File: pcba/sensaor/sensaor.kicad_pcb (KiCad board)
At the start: 2 copper layers, 55 x 29.5 mm, 16 parts, among them J1 SAO, J2 WS2812, J3 Conn_01x10_Pin, J4 Conn_01x10_Pin, J5 Conn_01x10_Pin, J6 Programming, J7 Conn_01x10_Pin, J8 Conn_01x10_Pin, J9 Conn_01x10_Pin, U1 CH32V003AxMx

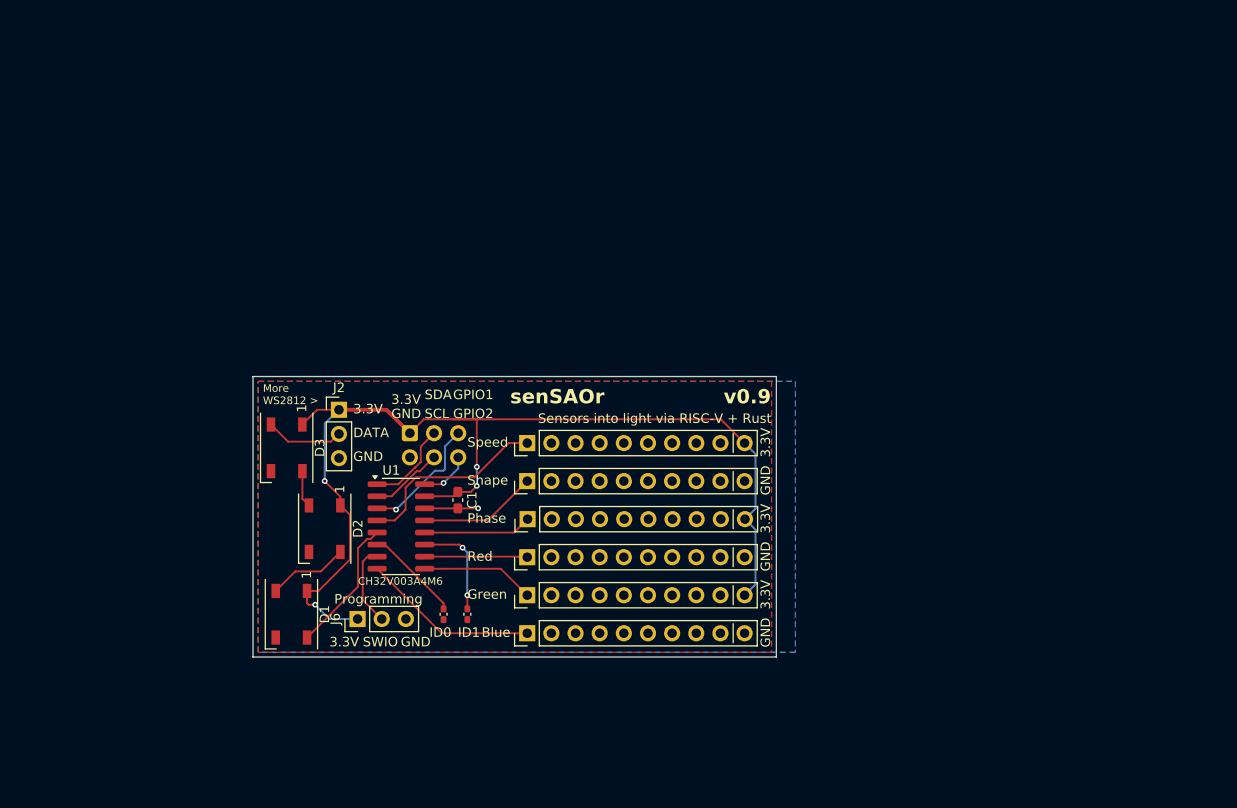
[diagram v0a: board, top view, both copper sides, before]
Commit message: Redesign board into more of a carrier shape
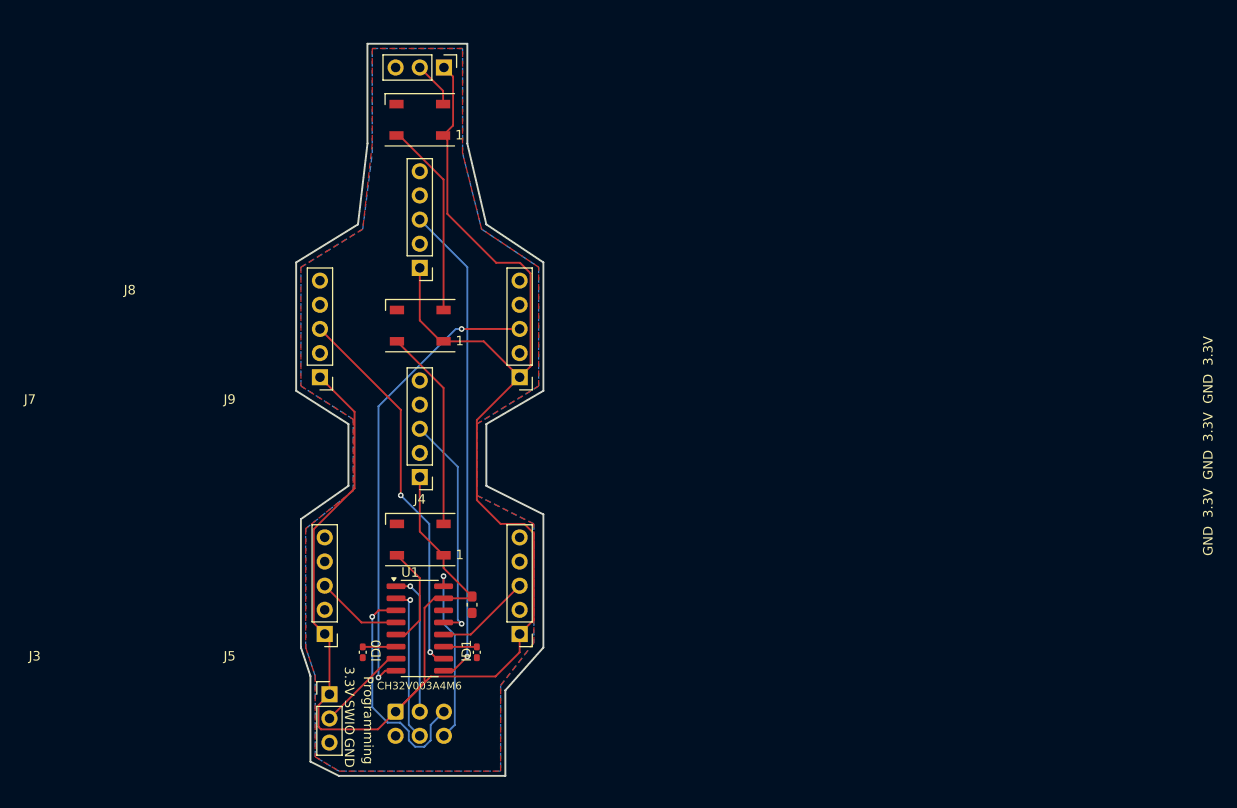
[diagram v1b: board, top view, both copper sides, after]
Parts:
- J3, J4, J5, J7, J8, J9: value Conn_01x10_Pin -> Conn_01x05_Pin; footprint Connector_PinHeader_2.54mm:PinHeader_1x10_P2.54mm_Vertical -> Connector_PinHeader_2.54mm:PinHeader_1x05_P2.54mm_Vertical
- moved J2 37.7 mm to (96.0, 20.5), turned to -90 degrees
- moved D3 37.2 mm to (93.5, 26.0), turned to 180 degrees
- moved J8 36.2 mm to (93.5, 41.6), turned to 180 degrees
- moved J1 29.3 mm to (91.0, 88.2)
- moved J3 29.3 mm to (83.5, 80.1), turned to 180 degrees
- moved J7 28.9 mm to (83.0, 53.1), turned to 180 degrees
- moved J9 26.9 mm to (104.0, 53.1), turned to 180 degrees
- moved D2 23.6 mm to (93.5, 47.6), turned to 180 degrees
- moved D1 15.7 mm to (93.5, 70.2), turned to 180 degrees
- moved J5 12.1 mm to (104.0, 80.1), turned to 180 degrees
- moved J4 11.3 mm to (93.5, 63.6), turned to 180 degrees
- moved C1 11.1 mm to (99.0, 77.0)
- moved U1 10.9 mm to (93.5, 79.5)
- moved R1 9.39 mm to (87.5, 82.0)
- moved J6 8.46 mm to (84.0, 86.4), turned to 0 degrees
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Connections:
- J3 pad 1: /SPEED -> VCC
- J3 pad 3: unconnected-(J3-Pin_3-Pad3) -> /SPEED
- J3 pad 5: unconnected-(J3-Pin_5-Pad5) -> GND
- J4 pad 1: /SHAPE -> VCC
- J4 pad 3: unconnected-(J4-Pin_3-Pad3) -> /SHAPE
- J4 pad 5: unconnected-(J4-Pin_5-Pad5) -> GND
- J5 pad 1: /PHASE -> VCC
- J5 pad 3: unconnected-(J5-Pin_3-Pad3) -> /PHASE
- J5 pad 5: unconnected-(J5-Pin_5-Pad5) -> GND
- J7 pad 1: /AR -> VCC
- J7 pad 3: unconnected-(J7-Pin_3-Pad3) -> /AR
- J7 pad 5: unconnected-(J7-Pin_5-Pad5) -> GND
- J8 pad 1: /AG -> VCC
- J8 pad 3: unconnected-(J8-Pin_3-Pad3) -> /AG
- J8 pad 5: unconnected-(J8-Pin_5-Pad5) -> GND
- J9 pad 1: /AB -> VCC
- J9 pad 3: unconnected-(J9-Pin_3-Pad3) -> /AB
- J9 pad 5: unconnected-(J9-Pin_5-Pad5) -> GND
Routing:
- net VCC: track 113.9 -> 192.3 mm, vias 4 -> 0
- net /AG: track 11.9 -> 51.1 mm, vias 0 -> 1
- net /AB: track 18.6 -> 48.9 mm, vias 0 -> 2
- net /AR: track 10.9 -> 40.5 mm, vias 0 -> 2
- net Net-(D2-DOUT): track 3.89 -> 20.6 mm
- net /GPIO2: track 5.37 -> 18.8 mm
- net Net-(D1-DOUT): track 8.50 -> 21.2 mm
- net /SHAPE: track 12.5 -> 24.3 mm, vias 0 -> 1
- net /SPEED: track 20.5 -> 9.10 mm
- net /GPIO1: track 13.3 -> 24.6 mm
- net /SCL: track 7.64 -> 16.4 mm, vias 0 -> 1
- net /ID1: track 10.9 -> 3.51 mm, vias 2 -> 0
- net GND: track 6.67 -> 0.00 mm, vias 1 -> 0
- net /ID0: track 10.1 -> 3.51 mm
- net /SDA: track 9.16 -> 15.1 mm, vias 0 -> 1
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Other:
- board size 55 x 29.5 mm -> 26 x 77 mm
- board text added: "v1.0"
- board text removed: "GPIO1"
- board text removed: "GPIO2"
- board text removed: "SCL"
- board text removed: "SDA"
- board text removed: "v0.9"

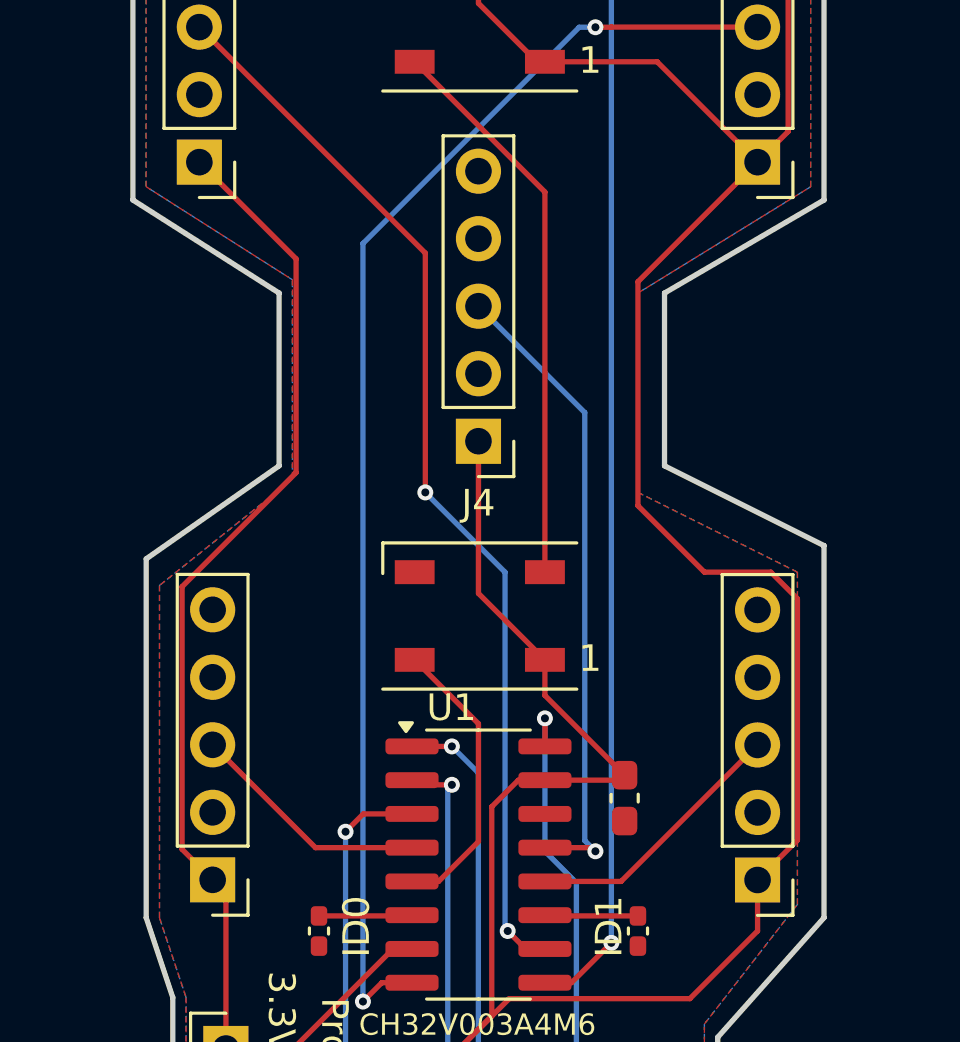
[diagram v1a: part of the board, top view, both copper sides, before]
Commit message: Fix ground plane connections
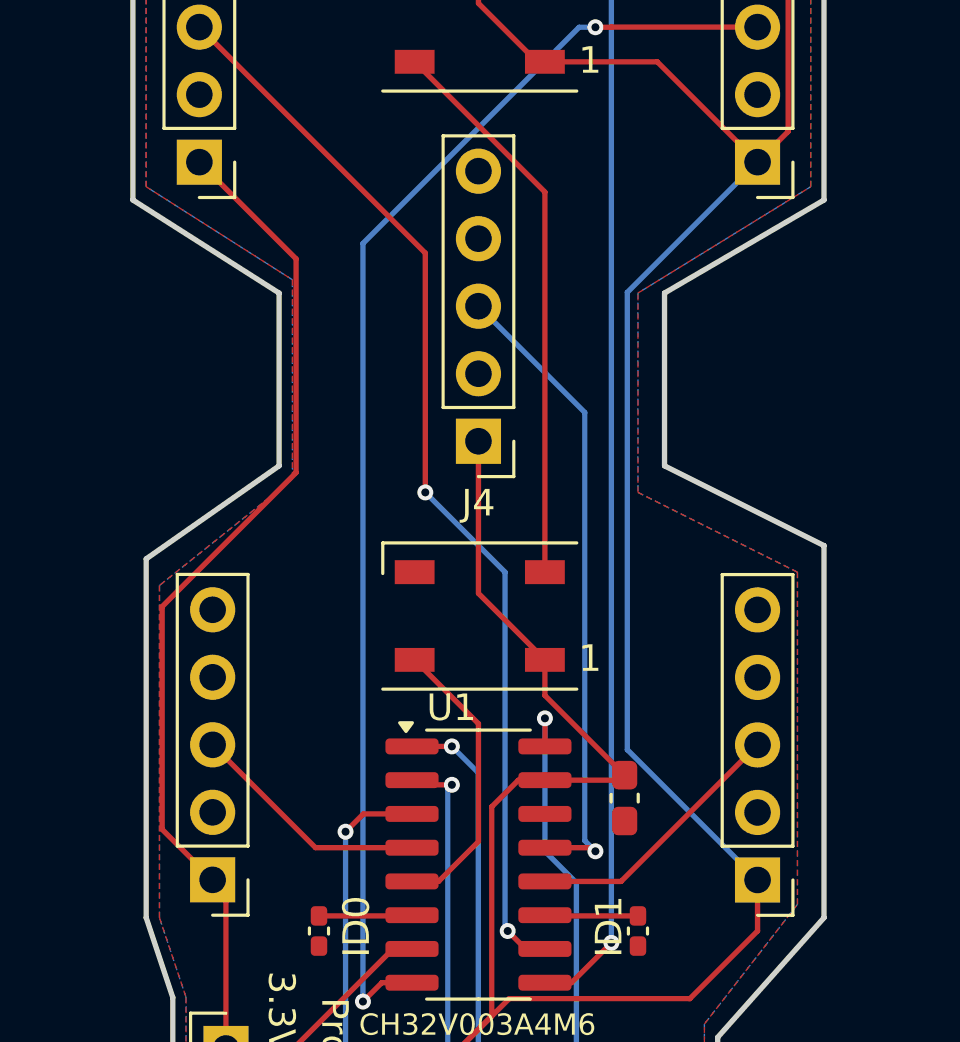
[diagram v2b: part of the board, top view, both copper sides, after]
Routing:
- net VCC: track 192.3 -> 190.5 mm
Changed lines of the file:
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@@
 	)
 	(segment
-		(start 105.5 69.5)
-		(end 104.5 68.5)
-		(width 0.2)
-		(layer "F.Cu")
-		(net 1)
-	)
-	(segment
-		(start 82.35 69.046697)
+		(start 81.6 69.796697)
 		(end 86.639626 64.757071)
 		(width 0.2)
@@
 	)
 	(segment
-		(start 104.5 68.5)
-		(end 102 68.5)
-		(width 0.2)
-		(layer "F.Cu")
-		(net 1)
-	)
-	(segment
 		(start 90.955 88.2475)
 		(end 94 85.2025)
@@
 	)
 	(segment
+		(start 97 26.6)
+		(end 97 21.46)
+		(width 0.2)
+		(layer "F.Cu")
+		(net 1)
+	)
+	(segment
+		(start 105.15 51.925)
+		(end 104 53.075)
+		(width 0.2)
+		(layer "F.Cu")
+		(net 1)
+	)
+	(segment
+		(start 97 21.46)
+		(end 96.04 20.5)
+		(width 0.2)
+		(layer "F.Cu")
+		(net 1)
+	)
+	(segment
+		(start 96 49.3)
+		(end 95.7 49.3)
+		(width 0.2)
+		(layer "F.Cu")
+		(net 1)
+	)
+	(segment
+		(start 105.15 42.15)
+		(end 105.15 51.925)
+		(width 0.2)
+		(layer "F.Cu")
+		(net 1)
+	)
+	(segment
+		(start 94 77.325001)
+		(end 95.000001 76.325)
+		(width 0.2)
+		(layer "F.Cu")
+		(net 1)
+	)
+	(segment
+		(start 81.6 78.175)
+		(end 81.6 69.796697)
+		(width 0.2)
+		(layer "F.Cu")
+		(net 1)
+	)
+	(segment
+		(start 96 71.8)
+		(end 96 73.1375)
+		(width 0.2)
+		(layer "F.Cu")
+		(net 1)
+	)
+	(segment
+		(start 96 73.1375)
+		(end 99 76.1375)
+		(width 0.2)
+		(layer "F.Cu")
+		(net 1)
+	)
+	(segment
+		(start 96.4 28.1)
+		(end 96.4 35.9)
+		(width 0.2)
+		(layer "F.Cu")
+		(net 1)
+	)
+	(segment
+		(start 84 80.575)
+		(end 83.5 80.075)
+		(width 0.2)
+		(layer "F.Cu")
+		(net 1)
+	)
+	(segment
+		(start 90.955 88.2475)
+		(end 94.6575 84.545)
+		(width 0.2)
+		(layer "F.Cu")
+		(net 1)
+	)
+	(segment
+		(start 93.5 63.575)
+		(end 93.5 69.3)
+		(width 0.2)
+		(layer "F.Cu")
+		(net 1)
+	)
+	(segment
+		(start 101.455 84.545)
+		(end 104 82)
+		(width 0.2)
+		(layer "F.Cu")
+		(net 1)
+	)
+	(segment
+		(start 96.4 35.9)
+		(end 101.537692 41.037692)
+		(width 0.2)
+		(layer "F.Cu")
+		(net 1)
+	)
+	(segment
+		(start 101.537692 41.037692)
+		(end 104.037692 41.037692)
+		(width 0.2)
+		(layer "F.Cu")
+		(net 1)
+	)
+	(segment
+		(start 98.8125 76.325)
+		(end 99 76.1375)
+		(width 0.2)
+		(layer "F.Cu")
+		(net 1)
+	)
+	(segment
+		(start 104.037692 41.037692)
+		(end 105.15 42.15)
+		(width 0.2)
+		(layer "F.Cu")
+		(net 1)
+	)
+	(segment
+		(start 104 82)
+		(end 104 80.08)
+		(width 0.2)
+		(layer "F.Cu")
+		(net 1)
+	)
+	(segment
+		(start 95.95 27.65)
+		(end 96.4 28.1)
+		(width 0.2)
+		(layer "F.Cu")
+		(net 1)
+	)
+	(segment
 		(start 86.639626 56.714626)
 		(end 83 53.075)
@@
 	)
 	(segment
-		(start 97 26.6)
-		(end 97 21.46)
-		(width 0.2)
-		(layer "F.Cu")
-		(net 1)
-	)
-	(segment
-		(start 105.15 51.925)
+		(start 96 76.325)
+		(end 98.8125 76.325)
+		(width 0.2)
+		(layer "F.Cu")
+		(net 1)
+	)
+	(segment
+		(start 100.225 49.3)
 		(end 104 53.075)
 		(width 0.2)
@@
 	)
 	(segment
-		(start 97 21.46)
-		(end 96.04 20.5)
+		(start 82.35 53.725)
+		(end 83 53.075)
 		(width 0.2)
 		(layer "F.Cu")
@@
 	(segment
 		(start 96 49.3)
-		(end 95.7 49.3)
+		(end 100.225 49.3)
+		(width 0.2)
+		(layer "F.Cu")
+		(net 1)
+	)
+	(segment
+		(start 89.0925 90.11)
+		(end 83.11 90.11)
 		(width 0.2)
 		(layer "F.Cu")
@@
 	(segment
 		(start 83.5 80.075)
-		(end 82.35 78.925)
-		(width 0.2)
-		(layer "F.Cu")
-		(net 1)
-	)
-	(segment
-		(start 105.15 42.15)
-		(end 105.15 51.925)
-		(width 0.2)
-		(layer "F.Cu")
-		(net 1)
-	)
-	(segment
-		(start 94 77.325001)
-		(end 95.000001 76.325)
-		(width 0.2)
-		(layer "F.Cu")
-		(net 1)
-	)
-	(segment
-		(start 96 71.8)
-		(end 96 73.1375)
-		(width 0.2)
-		(layer "F.Cu")
-		(net 1)
-	)
-	(segment
-		(start 96 73.1375)
-		(end 99 76.1375)
-		(width 0.2)
-		(layer "F.Cu")
-		(net 1)
-	)
-	(segment
-		(start 96.4 28.1)
-		(end 96.4 35.9)
-		(width 0.2)
-		(layer "F.Cu")
-		(net 1)
-	)
-	(segment
-		(start 84 80.575)
-		(end 83.5 80.075)
-		(width 0.2)
-		(layer "F.Cu")
-		(net 1)
-	)
-	(segment
-		(start 105.5 78.58)
-		(end 105.5 69.5)
-		(width 0.2)
-		(layer "F.Cu")
-		(net 1)
-	)
-	(segment
-		(start 99.5 57.575)
-		(end 104 53.075)
-		(width 0.2)
-		(layer "F.Cu")
-		(net 1)
-	)
-	(segment
-		(start 99.5 66)
-		(end 99.5 57.575)
-		(width 0.2)
-		(layer "F.Cu")
-		(net 1)
-	)
-	(segment
-		(start 90.955 88.2475)
-		(end 94.6575 84.545)
-		(width 0.2)
-		(layer "F.Cu")
-		(net 1)
-	)
-	(segment
-		(start 93.5 63.575)
-		(end 93.5 69.3)
-		(width 0.2)
-		(layer "F.Cu")
-		(net 1)
-	)
-	(segment
-		(start 101.455 84.545)
-		(end 104 82)
-		(width 0.2)
-		(layer "F.Cu")
-		(net 1)
-	)
-	(segment
-		(start 102 68.5)
-		(end 99.5 66)
-		(width 0.2)
-		(layer "F.Cu")
-		(net 1)
-	)
-	(segment
-		(start 96.4 35.9)
-		(end 101.537692 41.037692)
-		(width 0.2)
-		(layer "F.Cu")
-		(net 1)
-	)
-	(segment
-		(start 82.35 78.925)
-		(end 82.35 69.046697)
-		(width 0.2)
-		(layer "F.Cu")
-		(net 1)
-	)
-	(segment
-		(start 101.537692 41.037692)
-		(end 104.037692 41.037692)
-		(width 0.2)
-		(layer "F.Cu")
-		(net 1)
-	)
-	(segment
-		(start 98.8125 76.325)
-		(end 99 76.1375)
-		(width 0.2)
-		(layer "F.Cu")
-		(net 1)
-	)
-	(segment
-		(start 104.037692 41.037692)
-		(end 105.15 42.15)
-		(width 0.2)
-		(layer "F.Cu")
-		(net 1)
-	)
-	(segment
-		(start 104 82)
-		(end 104 80.08)
-		(width 0.2)
-		(layer "F.Cu")
-		(net 1)
-	)
-	(segment
-		(start 95.95 27.65)
-		(end 96.4 28.1)
-		(width 0.2)
-		(layer "F.Cu")
-		(net 1)
-	)
-	(segment
-		(start 104 80.08)
-		(end 105.5 78.58)
+		(end 81.6 78.175)
+		(width 0.2)
+		(layer "F.Cu")
+		(net 1)
+	)
+	(segment
+		(start 83.11 90.11)
+		(end 82.85 89.85)
 		(width 0.2)
 		(layer "F.Cu")
@@
 	)
 	(segment
-		(start 96 76.325)
-		(end 98.8125 76.325)
-		(width 0.2)
-		(layer "F.Cu")
-		(net 1)
-	)
-	(segment
-		(start 100.225 49.3)
-		(end 104 53.075)
-		(width 0.2)
-		(layer "F.Cu")
-		(net 1)
-	)
-	(segment
-		(start 82.35 53.725)
-		(end 83 53.075)
-		(width 0.2)
-		(layer "F.Cu")
-		(net 1)
-	)
-	(segment
-		(start 96 49.3)
-		(end 100.225 49.3)
-		(width 0.2)
-		(layer "F.Cu")
-		(net 1)
-	)
-	(segment
-		(start 89.0925 90.11)
-		(end 83.11 90.11)
-		(width 0.2)
-		(layer "F.Cu")
-		(net 1)
-	)
-	(segment
-		(start 83.11 90.11)
-		(end 82.85 89.85)
-		(width 0.2)
-		(layer "F.Cu")
-		(net 1)
-	)
+		(start 99.1 57.975)
+		(end 99.1 75.18)
+		(width 0.2)
+		(layer "B.Cu")
+		(net 1)
+	)
+	(segment
+		(start 99.1 75.18)
+		(end 104 80.08)
+		(width 0.2)
+		(layer "B.Cu")
+		(net 1)
+	)
+	(segment
+		(start 104 53.075)
+		(end 99.1 57.975)
+		(width 0.2)
+		(layer "B.Cu")
+		(net 1)
+	)

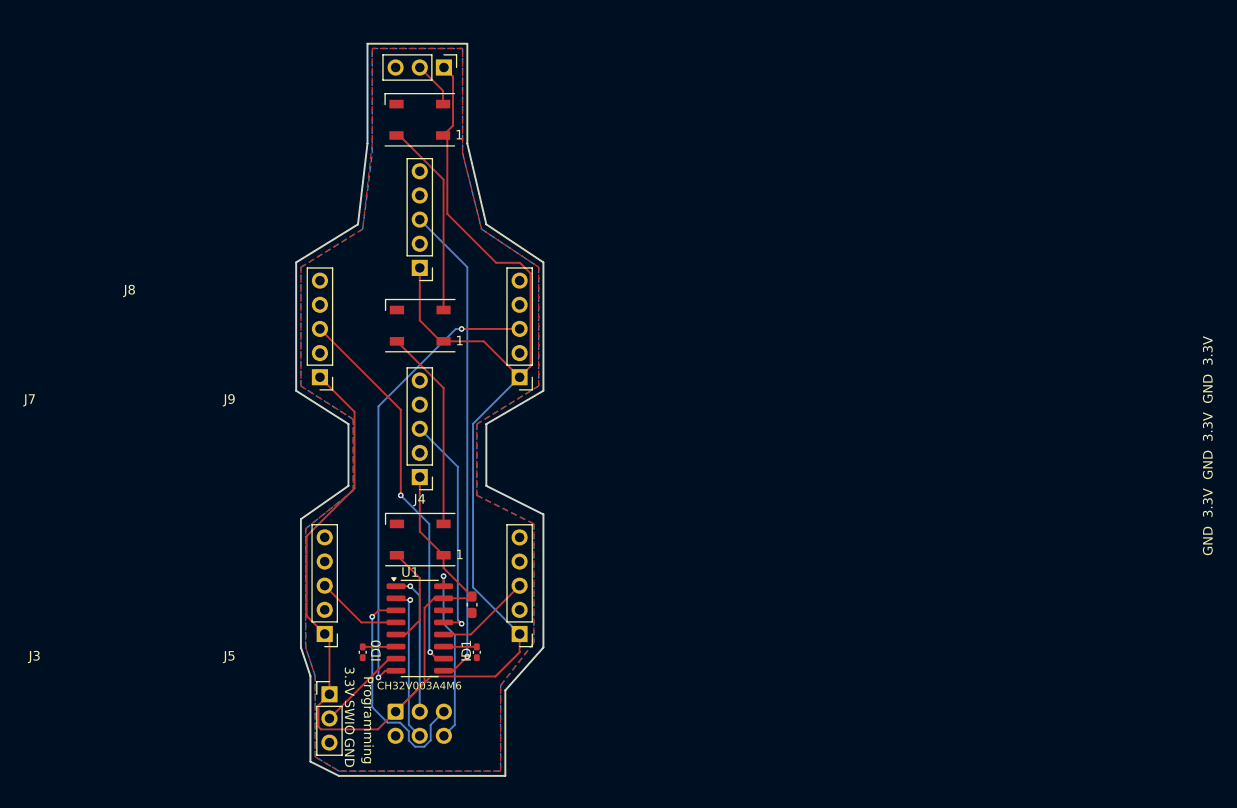
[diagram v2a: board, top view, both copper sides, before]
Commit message: Update silkscreens
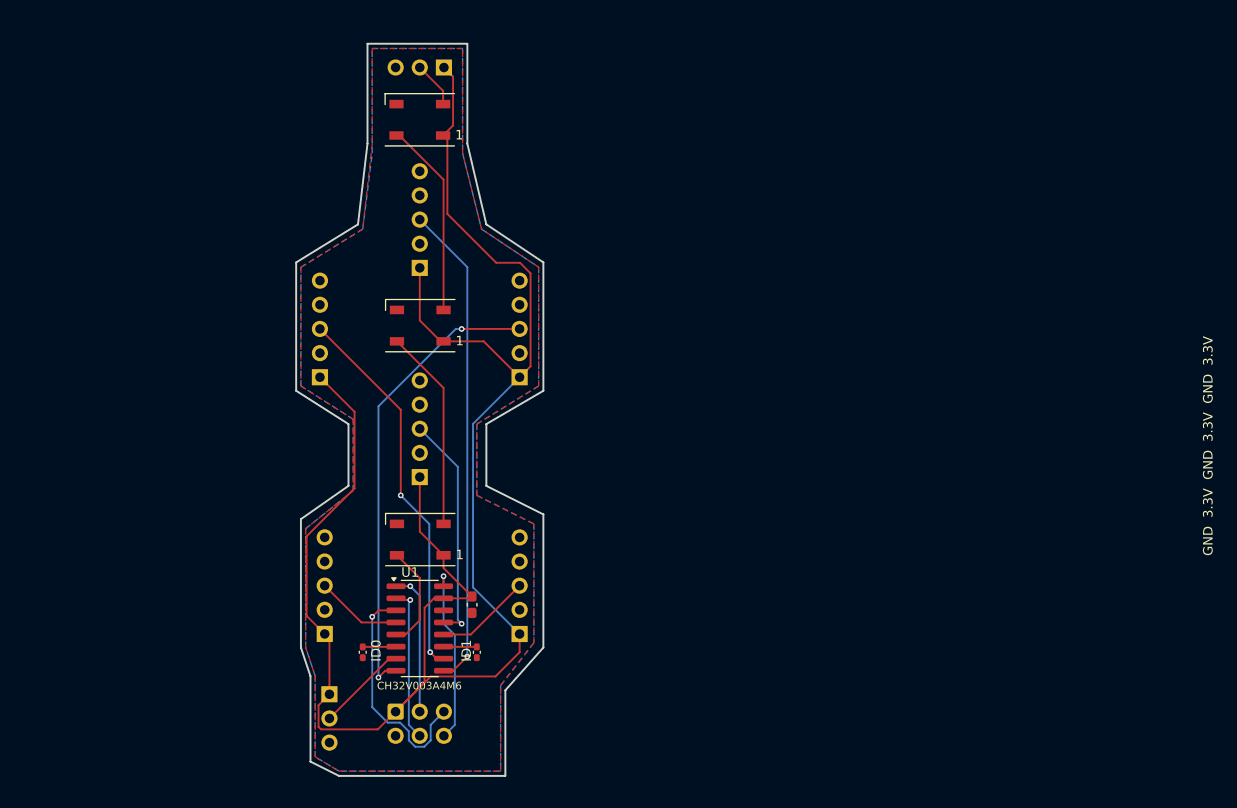
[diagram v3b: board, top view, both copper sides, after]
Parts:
- J2, J3, J4, J5, J6, J7, J8, J9: moved to B.Cu
- turned J2 to 90 degrees
- turned J3 to 0 degrees
- turned J4 to 0 degrees
- turned J5 to 0 degrees
- turned J6 to 180 degrees
- turned J7 to 0 degrees
- turned J8 to 0 degrees
- turned J9 to 0 degrees
